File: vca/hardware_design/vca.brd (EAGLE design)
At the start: 29.2 x 100 mm, 69 parts, among them IC1 LM13700M, IC2 TL074D

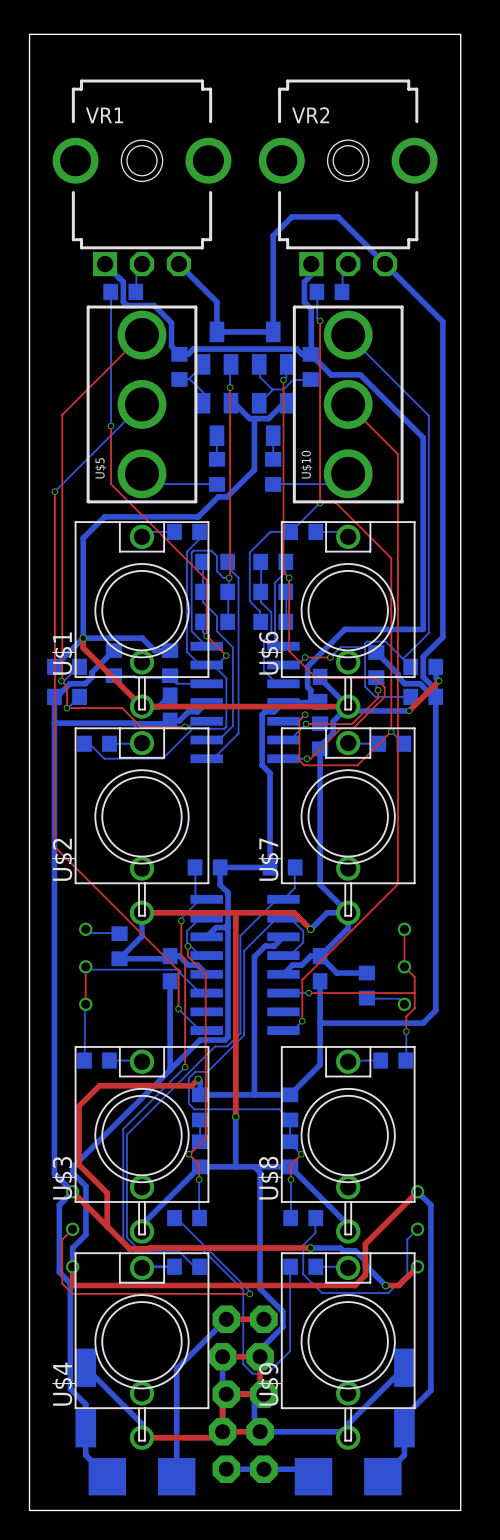
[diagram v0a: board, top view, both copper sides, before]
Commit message: Rename vca2 to vca, remove vca
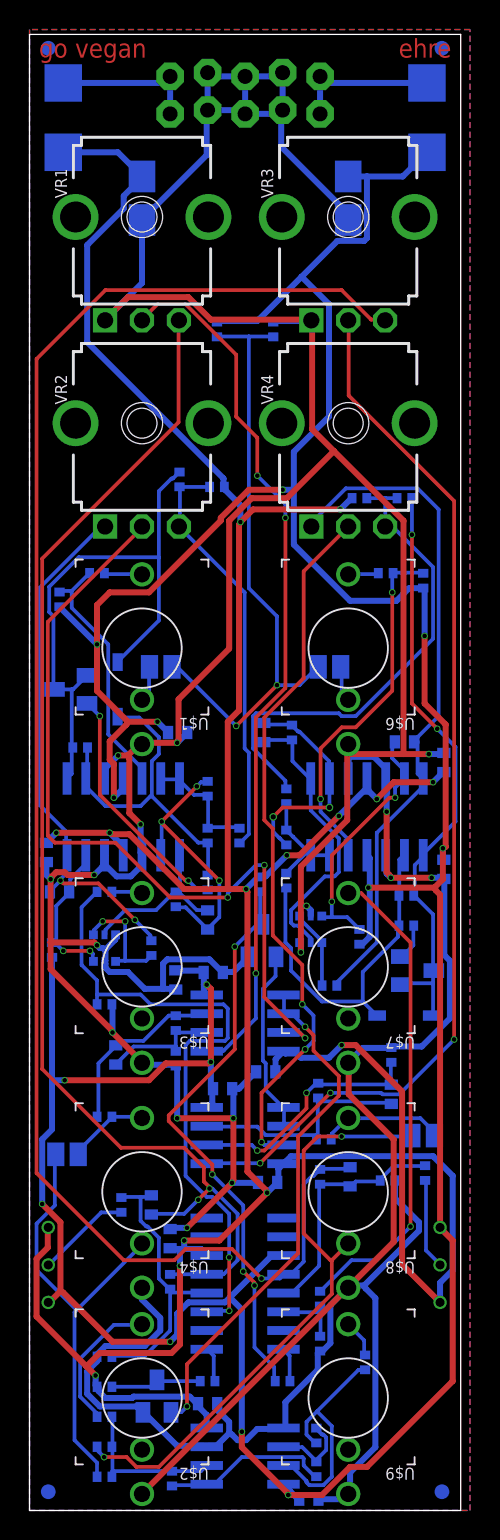
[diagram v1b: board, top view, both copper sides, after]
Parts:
- removed C6, C7: 22uF, rcl:PANASONIC_C
- removed U$10, U$5: INSTRUO_TOGGLE_ON_OFF_ON, Pure LFO:INSTRUO_TOGGLE_ON_OFF_ON
- added C10, C11, C14, C15: 22pF, jhbruhn-cr:C0402
- added C12, C13, C8, C9: 100pF, jhbruhn-cr:C0402
- added C16, C17, C18, C19, C20, C21, C22, C23: 100nF, jhbruhn-cr:C0402
- added C24, C25: 10uF, rcl:A/3216-18W
- added D3, D4: 1N4148-2, adafruit:SOD-123
- added FD1, FD2, FD3, FD4: FIDUCIAL1X2, SparkFun-Aesthetics:FIDUCIAL-1X2
- added IC4, U1, U2: TL072CD, jhbruhn-opamp:SOIC8
- added IC5: NCS20074D, ncs20074:SO14
- added LOGO1: OSHW-LOGOM, SparkFun-Aesthetics:OSHW-LOGO-M
- added R43: 68k, jhbruhn-cr:R0402
- added R44, R47: 1k, jhbruhn-cr:R0402
- added R45: 15k, jhbruhn-cr:R0402
- added R46: 680k, jhbruhn-cr:R0402
- added R48, R49, R50, R51, R52, R53: 100k, jhbruhn-cr:R0402
- added R54: 10k, jhbruhn-cr:R0402
- added R55: 50k, jhbruhn-cr:R0402
- added SJ1, SJ2, SJ3, SJ4: (no value), jumper:SJ
- added T5: BC847BS, nxp_60:SOT363
- added T6: 2N3906, transistor-neu-to92:SOT23-BEC
- added VR3, VR4: 100k, jhbruhn-physical:9MM_SNAP-IN_POT
- C1: device MusicThingModular:EURO_PWR_HEADER_LOCK -> jhbruhn-physical:EURO_PWR_HEADER_LOCK
- C2, C3, C4, C5: device rcl:C0603 -> jhbruhn-cr:C0402
- IC1: device ota:SO16 -> jhbruhn-ota:SO16
- IC2: value TL074D -> NCS20074D; device linear:SO14 -> ncs20074:SO14
- R1, R21, R24: value 100k -> 1k; device rcl:R0603 -> jhbruhn-cr:R0402
- R10: value 470 -> 10k; device rcl:R0603 -> jhbruhn-cr:R0402
- R11: value 100k -> 10M; device rcl:R0603 -> jhbruhn-cr:R0402
- R12: value 100k -> 1k5; device rcl:R0603 -> jhbruhn-cr:R0402
- R13: value 2k -> 100k; device rcl:RTRIM64W -> jhbruhn-cr:R0402
- R14: value 150 -> 680R; device rcl:R0603 -> jhbruhn-cr:R0402
- R15: value 2M -> 47k; device rcl:R0603 -> jhbruhn-cr:R0402
- R16: value 470k -> 680R; device rcl:R0603 -> jhbruhn-cr:R0402
- R17: value 47k -> 1M; device rcl:R0603 -> jhbruhn-cr:R0402
- R18: value 4k7 -> 100k; device rcl:R0603 -> rcl:RTRIM64W
- R19: value 1k -> 100k; device rcl:R0603 -> jhbruhn-cr:R0402
- R2, R3: value 100k -> 1M; device rcl:R0603 -> jhbruhn-cr:R0402
- R20: value 20k -> 68k; device rcl:R0603 -> jhbruhn-cr:R0402
- R22: value 100k -> 15k; device rcl:R0603 -> jhbruhn-cr:R0402
- R23: value 100k -> 680k; device rcl:R0603 -> jhbruhn-cr:R0402
- R25, R26: value 2k -> 1M; device rcl:R0603 -> jhbruhn-cr:R0402
- R27: value 120k -> 100k; device rcl:R0603 -> jhbruhn-cr:R0402
- R28, R5: value 2k -> 100k; device rcl:R0603 -> jhbruhn-cr:R0402
- R29: value 100k -> 220R; device rcl:R0603 -> jhbruhn-cr:R0402
- R30: value 470 -> 220R; device rcl:R0603 -> jhbruhn-cr:R0402
- R31: value 100k -> 56k; device rcl:R0603 -> jhbruhn-cr:R0402
- R32, R9: value 100k -> 33k; device rcl:R0603 -> jhbruhn-cr:R0402
- R33: value 2k -> 10k; device rcl:RTRIM64W -> jhbruhn-cr:R0402
- R34: value 150 -> 10M; device rcl:R0603 -> jhbruhn-cr:R0402
- R35: value 2M -> 1k5; device rcl:R0603 -> jhbruhn-cr:R0402
- R36: value 470k -> 100k; device rcl:R0603 -> jhbruhn-cr:R0402
- R37: value 47k -> 680R; device rcl:R0603 -> jhbruhn-cr:R0402
- R38: value 4k7 -> 47k; device rcl:R0603 -> jhbruhn-cr:R0402
- R39: value 1k -> 680R; device rcl:R0603 -> jhbruhn-cr:R0402
- R4: device rcl:R0603 -> jhbruhn-cr:R0402
- R40: value 20k -> 1M; device rcl:R0603 -> jhbruhn-cr:R0402
- R42: device rcl:RTRIM64W -> jhbruhn-cr:R0402
- R6: value 2k -> 220R; device rcl:R0603 -> jhbruhn-cr:R0402
- R7: value 120k -> 220R; device rcl:R0603 -> jhbruhn-cr:R0402
- R8: value 2k -> 56k; device rcl:R0603 -> jhbruhn-cr:R0402
- T1, T3, T4: value (none) -> 2N3906
- T2: value (none) -> BC847BS; device transistor-neu-to92:SOT23-BEC -> nxp_60:SOT363
- U$1, U$2, U$3, U$4, U$6, U$7, U$8, U$9: device thonkiconn:WQP-PJ301M-12_JACK -> jhbruhn-physical:WQP-PJ301M-12_JACK
- VR1, VR2: device MusicThingModular:9MM_SNAP-IN_POT -> jhbruhn-physical:9MM_SNAP-IN_POT
- moved D1 94.1 mm to (26.9, 94.4), turned to 90 degrees
- moved D2 94.1 mm to (2.29, 94.4), turned to 270 degrees
- moved C1 88.1 mm to (14.6, 96.0), turned to 180 degrees
- moved R23 75.7 mm to (5.08, 8.38), turned to 180 degrees
- moved T3 71.4 mm to (8.64, 7.75)
- moved R40 48.6 mm to (26.8, 22.9)
- moved R22 44.9 mm to (12.1, 8.76)
- moved R21 41.8 mm to (5.08, 26.7)
- moved R20 39.8 mm to (9.91, 30.6), turned to 270 degrees
- moved U$2 39.4 mm to (7.62, 7.62)
- moved T4 38.6 mm to (26.3, 36.6), turned to 90 degrees
- moved R32 38.2 mm to (22.4, 68.6)
- moved T2 36.6 mm to (5.08, 38.1)
- moved R7 35.0 mm to (12.1, 42.5)
- moved R27 34.8 mm to (17.4, 42.7)
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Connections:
- new net CHANNEL_A: R21.1, SJ1.2, U$4.P$1_TIP
- new net CHANNEL_A_OUT: R50.1, SJ1.1, U$4.P$2_SWITCH
- new net CHANNEL_B: R44.1, SJ2.2, U$8.P$1_TIP
- new net CHANNEL_B_OUT: R51.1, SJ2.1, U$8.P$2_SWITCH
- new net N$43: C14.1, IC1.12, R38.2, VR3.3
- new net N$44: R40.1, R41.2
- new net N$45: C15.2, R42.2, R43.1, U2.6
- new net N$46: U2.5, VR3.2
- new net N$47: C15.1, R42.1, R44.2, U2.7
- new net N$48: IC4.6, R48.1, R49.2
- new net N$49: T6.B, U2.1, U2.2
- new net N$50: U2.3, VR4.2
- new net N$51: IC1.16, R45.2
- new net N$52: R45.1, R46.2, T6.C
- new net N$53: IC4.1, R49.1, R52.2
- new net N$54: IC4.7, R47.2, R48.2
- new net N$55: IC4.2, R50.2, R51.2, R52.1, R53.2
- new net N$56: SJ3.2, U$1.P$2_SWITCH
- new net N$57: R53.1, U$2.P$1_TIP
- new net N$58: SJ4.2, U$6.P$2_SWITCH
- new net REF_10: R54.1, R55.2, SJ3.1, SJ4.1
- net +12V: now also C16.1, C18.1, C20.1, C22.1, C24.+, IC4.8, IC5.4, R11.2, R18.1, R2.2, R25.2, R34.2, R41.1, R54.2, U1.8, U2.8; no longer C6.+, R16.1, R24.1, R29.1, R36.1, R4.1, R41.3, R42.3, R9.1, T1.C, T3.C, VR1.3, VR2.3
- net -12V: now also C17.2, C19.2, C21.2, C23.2, C25.-, IC4.4, IC5.11, R18.3, R23.1, R32.1, R41.3, R46.1, R9.1, U1.4, U2.4; no longer C7.-, R18.1, R27.1, R38.1, R41.1, R42.1, R7.1, VR1.1, VR2.1
- net GND: now also C16.2, C17.1, C18.2, C19.1, C20.2, C21.1, C22.2, C23.1, C24.-, C25.+, IC2.10, IC2.12, IC2.3, IC4.3, IC4.5, IC5.10, IC5.12, IC5.3, R16.1, R20.2, R37.1, R39.1, R43.2, R55.1, T2.3, T2.5, T3.E, T5.3, T5.5, T6.E, U$1.P$3_SLEEVE, U$2.P$3_SLEEVE, U$3.P$3_SLEEVE, U$4.P$3_SLEEVE, U$6.P$3_SLEEVE, U$7.P$3_SLEEVE, U$8.P$3_SLEEVE, U$9.P$3_SLEEVE, VR1.1, VR3.1; no longer C6.-, C7.+, IC1.13, IC1.4, R10.2, R17.2, R25.2, R30.2, R34.1, R37.2, R5.2, T2.E, T4.E, U$1.P$3, U$2.P$3, U$3.P$3, U$4.P$3, U$6.P$3, U$7.P$3, U$8.P$3, U$9.P$3
- net N$1: now also IC2.5, R1.2, R2.1; no longer R1.1, U$1.P$1
- net N$10: now also C10.2, IC1.4, R15.1, R17.2; no longer IC1.5, IC1.7, R15.2, R17.1
- net N$11: now also D3.C, IC2.2, R4.2, R5.1, R7.1; no longer IC2.1, R11.2
- net N$12: now also R12.2, T2.1, T2.4; no longer R12.1, U$3.P$1
- net N$13: now also C9.1, IC2.14, R12.1, VR2.1; no longer IC1.3, R12.2, R13.2, R13.3
- net N$14: now also R13.1, U$3.P$1_TIP; no longer R15.1, R41.2
- net N$15: now also IC1.3, R13.2; no longer R13.1
- net N$16: now also R47.1, U$9.P$1_TIP; no longer R19.2, U$4.P$1
- net N$17: now also C10.1, IC1.5, R15.2, VR1.3; no longer IC1.8, R18.2, R19.1
- net N$18: now also R17.1, R18.2; no longer R20.1, U$5.1
- net N$19: now also U1.5, VR1.2; no longer IC1.1, U$5.2
- net N$2: now also C8.2, IC2.9, R10.1, R3.2; no longer R2.1, U$2.P$1
- net N$20: now also C11.2, R19.2, R20.1, U1.6; no longer R20.2, T2.C
- net N$21: now also IC5.5, R24.2, R25.1; no longer R21.1, U$6.P$1
- net N$22: now also C11.1, R19.1, R21.2, U1.7; no longer R22.1, U$7.P$1
- net N$23: now also T3.B, U1.1, U1.2; no longer R23.1, VR2.2
- net N$24: now also U1.3, VR2.2; no longer IC2.12, R21.2, R22.2, R23.2, R26.1
- net N$25: now also IC1.1, R22.2; no longer IC2.13, R24.2, R25.1
- net N$26: now also R22.1, R23.2, T3.C; no longer IC2.14, R26.2, R28.1, T3.B
- net N$27: now also C12.2, IC5.9, R26.2, R33.1; no longer R27.2, T3.E, T4.B
- net N$28: now also IC5.6, IC5.7, R26.1, R27.1; no longer IC2.10, R28.2
- net N$29: now also R24.1, U$6.P$1_TIP; no longer IC2.9, R29.2, R30.1, U$10.3
- net N$3: now also IC2.6, IC2.7, R4.1, R8.1; no longer VR1.2
- net N$30: now also R29.2, R32.2, VR4.3; no longer IC2.8
- net N$31: now also R30.2, T4.E; no longer IC1.10, IC1.12, R35.2, R36.2, R37.1
- net N$32: now also D4.A, IC5.1, R28.2, R29.1, T4.B, T4.C; no longer R32.1, U$8.P$1
- net N$33: now also D4.C, IC5.2, R27.2, R28.1, R30.1; no longer IC1.14, R32.2, R33.2, R33.3
- net N$34: now also C12.1, IC5.8, R33.2, T5.2; no longer R33.1, R34.2
- net N$35: now also R35.2, T5.1, T5.4; no longer R35.1, R42.2
- net N$36: now also C13.2, IC5.13, R34.1, T5.6; no longer R39.2, U$9.P$1
- net N$37: now also C13.1, IC5.14, R35.1, VR4.1; no longer IC1.9, R38.2, R39.1
- net N$38: now also R36.1, U$7.P$1_TIP; no longer R40.2, T4.C
- net N$39: now also IC1.14, R36.2, R37.2; no longer R40.1, U$10.1
- net N$4: now also R1.1, U$1.P$1_TIP; no longer IC2.6, R1.2, R2.2, R3.2, R6.1
- net N$40: now also C14.2, IC1.13, R38.1, R39.2, R40.2; no longer IC1.16, U$10.2
- net N$5: now also C8.1, IC2.8, R10.2, T2.2; no longer IC2.5, R4.2, R5.1
- net N$6: now also C9.2, IC2.13, R11.1, T2.6; no longer IC2.7, R6.2, R8.1, T1.B
- net N$7: now also R6.2, R9.2, VR2.3; no longer IC2.2, R11.1
- net N$8: no longer T2.B
- net N$9: now also D3.A, IC2.1, R5.2, R6.1, T1.B, T1.C; no longer IC2.3, R10.1, R9.2, U$5.3
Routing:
- net GND: track 219.5 -> 374.3 mm, vias 5 -> 17
- net N$43: track 0.00 -> 112.6 mm, vias 0 -> 1
- net N$46: track 0.00 -> 72.0 mm, vias 0 -> 3
- net N$4: track 56.8 -> 2.59 mm, vias 3 -> 0
- net -12V: track 168.3 -> 222.1 mm, vias 0 -> 14
- net N$17: track 34.6 -> 85.3 mm
- net N$50: track 0.00 -> 48.5 mm, vias 0 -> 3
- net REF_10: track 0.00 -> 41.5 mm, vias 0 -> 2
- net CHANNEL_B_OUT: track 0.00 -> 41.4 mm, vias 0 -> 2
- net N$15: track 2.43 -> 43.8 mm, vias 0 -> 2
- net N$52: track 0.00 -> 39.1 mm, vias 0 -> 4
- net N$29: track 41.1 -> 2.10 mm, vias 2 -> 0
- net N$32: track 2.24 -> 40.4 mm, vias 0 -> 2
- net N$26: track 39.6 -> 6.24 mm, vias 3 -> 0
- net N$23: track 2.09 -> 35.3 mm, vias 0 -> 2
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- added copper zone on layer 1, net GND
- added copper zone on layer 16, net GND
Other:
- board text added: "2VCA v1"
- board text added: "FCK AFD"
- board text added: "based on befaco hexmix vca"
- board text added: "ehre"
- board text added: "go vegan"
- board text added: "jhbruhn 2020"
